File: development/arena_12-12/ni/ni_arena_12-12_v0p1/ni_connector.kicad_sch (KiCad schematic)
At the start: 1 part, among them P13 CONN_34X2

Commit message: Worked on 12-12 ni arena.
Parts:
- removed P13: CONN_34X2, symbol arena_custom:CONN_34X2
- added J2: NI_TE_68pos, symbol arena_custom:NI_TE_68pos_2-5174225-5
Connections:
- net GND: now also J2.1 (Pin_1), J2.2 (Pin_2), J2.3 (Pin_3), J2.69 (GND), J2.70 (GND)
- net PAN3V.EXT_INT: now also J2.35 (Pin_35)
- net PAN3V.RESET: now also J2.34 (Pin_34)
- new net PAN3V.CS_00: J2.68 (Pin_68)
- new net PAN3V.CS_01: J2.67 (Pin_67)
- new net PAN3V.CS_02: J2.66 (Pin_66)
- new net PAN3V.CS_03: J2.65 (Pin_65)
- new net PAN3V.CS_04: J2.64 (Pin_64)
- new net PAN3V.CS_05: J2.63 (Pin_63)
- new net PAN3V.CS_06: J2.62 (Pin_62)
- new net PAN3V.CS_07: J2.61 (Pin_61)
- new net PAN3V.MISO_00: J2.53 (Pin_53)
- new net PAN3V.MISO_01: J2.51 (Pin_51)
- new net PAN3V.MISO_02: J2.49 (Pin_49)
- new net PAN3V.MISO_03: J2.47 (Pin_47)
- new net PAN3V.MISO_04: J2.45 (Pin_45)
- new net PAN3V.MISO_05: J2.43 (Pin_43)
- new net PAN3V.MISO_06: J2.41 (Pin_41)
- new net PAN3V.MISO_07: J2.40 (Pin_40)
- new net PAN3V.MISO_08: J2.39 (Pin_39)
- new net PAN3V.MISO_09: J2.38 (Pin_38)
- new net PAN3V.MISO_10: J2.37 (Pin_37)
- new net PAN3V.MISO_11: J2.36 (Pin_36)
- new net PAN3V.MOSI_00: J2.54 (Pin_54)
- new net PAN3V.MOSI_01: J2.52 (Pin_52)
- new net PAN3V.MOSI_02: J2.50 (Pin_50)
- new net PAN3V.MOSI_03: J2.48 (Pin_48)
- new net PAN3V.MOSI_04: J2.46 (Pin_46)
- new net PAN3V.MOSI_05: J2.44 (Pin_44)
- new net PAN3V.MOSI_06: J2.42 (Pin_42)
- new net PAN3V.MOSI_07: J2.29 (Pin_29)
- new net PAN3V.MOSI_08: J2.30 (Pin_30)
- new net PAN3V.MOSI_09: J2.31 (Pin_31)
- new net PAN3V.MOSI_10: J2.32 (Pin_32)
- new net PAN3V.MOSI_11: J2.33 (Pin_33)
- new net PAN3V.SCK_00: J2.60 (Pin_60)
- new net PAN3V.SCK_01: J2.59 (Pin_59)
- new net PAN3V.SCK_02: J2.58 (Pin_58)
- new net PAN3V.SCK_03: J2.57 (Pin_57)
- new net PAN3V.SCK_04: J2.56 (Pin_56)
- new net PAN3V.SCK_05: J2.55 (Pin_55)
- no-connect marks 38 -> 25

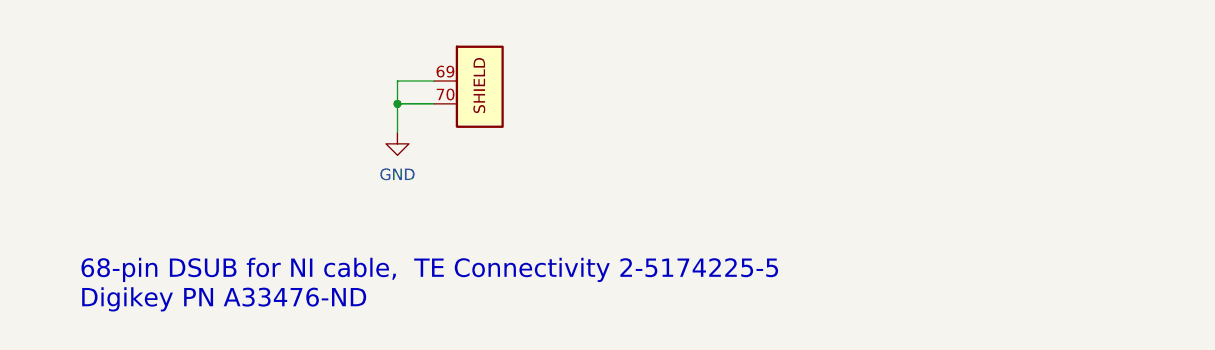
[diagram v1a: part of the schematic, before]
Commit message: Finished initial schematic and layout for 12-12 NI arena (without voltage regulators).
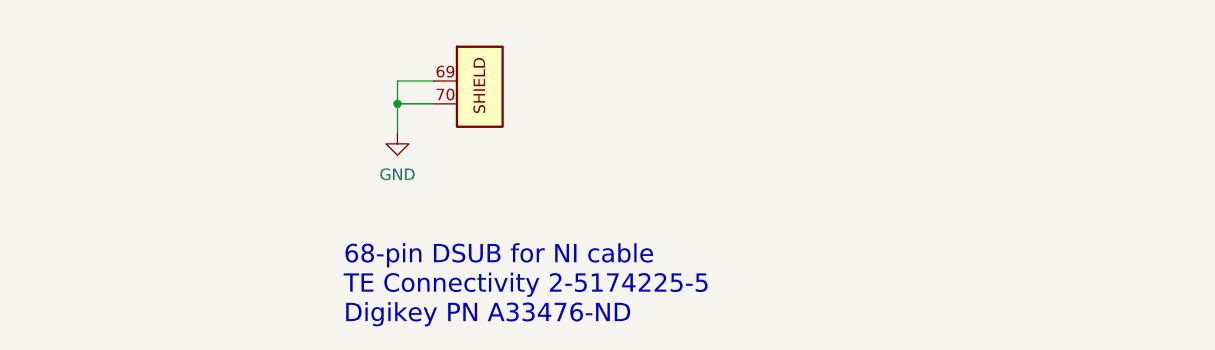
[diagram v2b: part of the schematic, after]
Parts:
- J2: footprint (none) -> arena_custom:TE_CONN_DSUB_RA_68
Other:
- note added: "68-pin DSUB for NI cable TE Connectivity 2-5174225-5 Digikey PN A33476-ND"
- note removed: "68-pin DSUB for NI cable, TE Connectivity 2-5174225-5 Digikey PN A33476-ND"

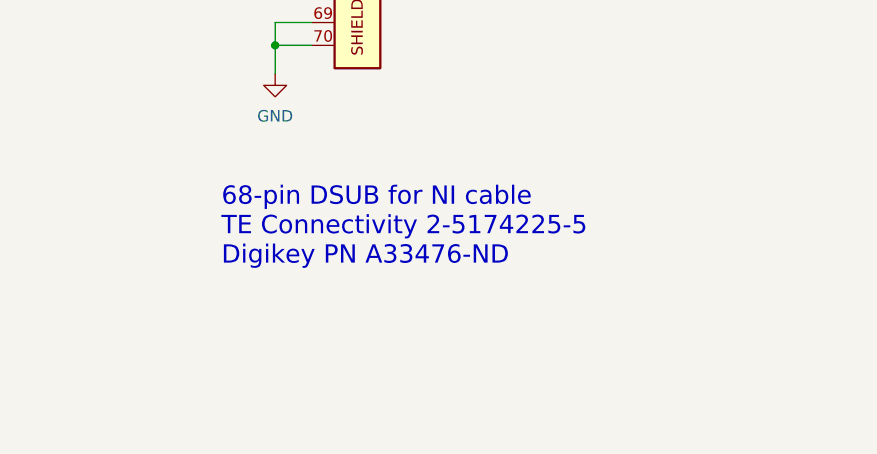
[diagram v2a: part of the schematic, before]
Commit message: Worked on 12-12 arenas.
Resized 12-12 arenas,   changed NI connector from right angle to
vertical, push panals back by 1mm.
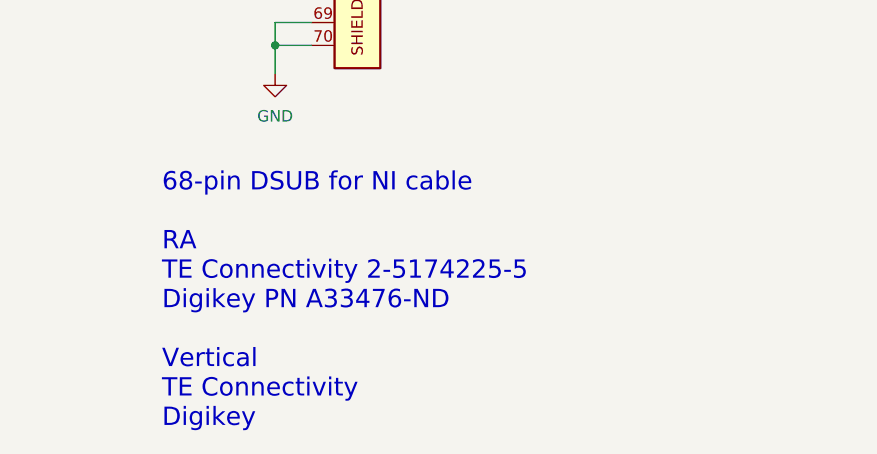
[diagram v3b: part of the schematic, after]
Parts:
- J2: footprint arena_custom:TE_CONN_DSUB_RA_68 -> arena_custom:TE_CONN_DSUB_VERT_68
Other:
- note added: "68-pin DSUB for NI cable RA TE Connectivity 2-5174225-5 Digikey PN A33476-ND Vertical TE Connectivity Digikey"
- note removed: "68-pin DSUB for NI cable TE Connectivity 2-5174225-5 Digikey PN A33476-ND"
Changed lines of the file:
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@@
     (stroke (width 0) (type default))
   )
-  (text "68-pin DSUB for NI cable  \nTE Connectivity 2-5174225-5\nDigikey PN A33476-ND"
-    (at 81.534 159.004 0)
+  (text "68-pin DSUB for NI cable  \n\nRA\nTE Connectivity 2-5174225-5\nDigikey PN A33476-ND\n\nVertical\nTE Connectivity \nDigikey "
+    (at 74.93 177.038 0)
     (effects (font (size 2.032 2.032)) (justify left bottom))
   )
@@
       (effects (font (size 1.27 1.27)))
     )
-    (property "Footprint" "arena_custom:TE_CONN_DSUB_RA_68" (at 95.377 77.216 0)
+    (property "Footprint" "arena_custom:TE_CONN_DSUB_VERT_68" (at 95.377 77.216 0)
       (effects (font (size 1.27 1.27)) hide)
     )

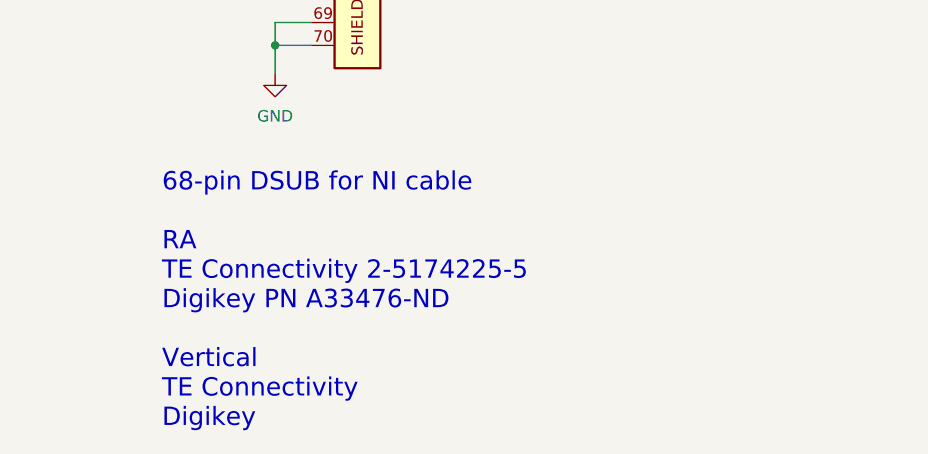
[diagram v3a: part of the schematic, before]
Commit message: Work on BOMs for 12-12 arenas with vregs. Finish non-LSCS versions.
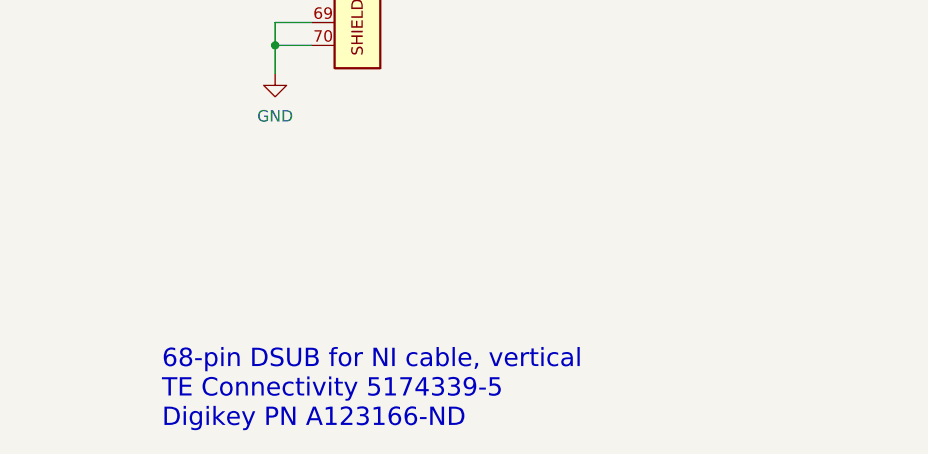
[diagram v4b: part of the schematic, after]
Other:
- note added: "68-pin DSUB for NI cable, vertical TE Connectivity 5174339-5 Digikey PN A123166-ND"
- note removed: "68-pin DSUB for NI cable RA TE Connectivity 2-5174225-5 Digikey PN A33476-ND Vertical TE Connectivity Digikey"
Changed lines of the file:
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@@
     (stroke (width 0) (type default))
   )
-  (text "68-pin DSUB for NI cable  \n\nRA\nTE Connectivity 2-5174225-5\nDigikey PN A33476-ND\n\nVertical\nTE Connectivity \nDigikey "
+  (text "68-pin DSUB for NI cable, vertical  \nTE Connectivity 5174339-5\nDigikey PN A123166-ND\n"
     (at 74.93 177.038 0)
     (effects (font (size 2.032 2.032)) (justify left bottom))
